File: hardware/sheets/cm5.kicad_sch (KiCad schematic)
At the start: 30 parts, among them J3 microSD, J4 RJ45 GbE magjack UDE RB1-125B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, J40 Fan GND/5V/TACH/PWM, J41 OLED GND/VCC/SCL/SDA, J5 USB-C rpiboot, J6 nRPIBOOT, J7 UART0 GND/TX/RX, M1 CM5002016, Q1 2N7002, SW1 DIP x8, U52 TPS22965DSGR

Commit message: design v2: wireless brain box (C22-C23) — no Ethernet, no buzzer, passive cooler, hinged lid, Wi-Fi AP + QR + phone page, fabrication guide
hardware: 136x100 outline, CM5 wireless antenna edge on the left board edge with a copper-free
strip (rule area), DIN/USB-C/microSD on the right wall, M.2 along the front under the lid, lid
microswitch, CR2032 + service headers on the bottom; magjack and buzzer removed from the
netlist; check_place clean, DRC 0 errors; schematic + connections regenerated, render script
also exports the schematic
software: wifi.py (nmcli / simulated backends, ephemeral key, join, resets), webui.py (stdlib
HTTP phone page: status, certificates, log, join, reset), qr.py, OLED frames with the Wi-Fi QR
code, DIP mode 110 = SERVICE, braindrain wifi-reset; 74 tests, ruff clean; qrcode dependency
enclosure: hinged lid (rear knuckles, filament pin, front snap latch), vents on the antenna side
and front, right-wall cutouts, lid-open scene render
docs: C22/C23, FABRICATION.md (vendors, cost estimate, gates), STATUS R19-R20, panels rear/right,
OLED Wi-Fi mockup, README/ARCHITECTURE/USAGE/BOM/CHANGELOG/HISTORY/tracker updated

Co-Authored-By: Claude Fable 5.1 <noreply@anthropic.com>
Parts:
- removed R10, R11: 10k, Resistor_SMD:R_0402_1005Metric, symbol Device:R
- removed R2, R3: 1k, Resistor_SMD:R_0603_1608Metric, symbol Device:R
- removed R4: 1k, Resistor_SMD:R_0402_1005Metric, symbol Device:R
- removed R5: 100k, Resistor_SMD:R_0402_1005Metric, symbol Device:R
- removed R6, R7: 470, Resistor_SMD:R_0402_1005Metric, symbol Device:R
- BT1: renamed from J41; value OLED GND/VCC/SCL/SDA -> CR2032; footprint Connector_PinHeader_2.54mm:PinHeader_1x04_P2.54mm_Vertical -> Battery:BatteryHolder_Keystone_1060_1x2032; symbol Connector_Generic:Conn_01x04 -> Device:Battery_Cell
- C1: renamed from BT1; value CR2032 -> 22u 10V; footprint Battery:BatteryHolder_Keystone_1060_1x2032 -> Capacitor_SMD:C_0805_2012Metric; symbol Device:Battery_Cell -> Device:C
- C2: renamed from J6; value nRPIBOOT -> 22u 10V; footprint Connector_PinHeader_2.54mm:PinHeader_1x02_P2.54mm_Vertical -> Capacitor_SMD:C_0805_2012Metric; symbol Connector_Generic:Conn_01x02 -> Device:C
- C3: renamed from C1; value 22u 10V -> 10u 10V
- C4: renamed from C2; value 22u 10V -> 1u 10V; footprint Capacitor_SMD:C_0805_2012Metric -> Capacitor_SMD:C_0402_1005Metric
- D1: renamed from C3; value 10u 10V -> green PWR; footprint Capacitor_SMD:C_0805_2012Metric -> LED_THT:LED_D3.0mm; symbol Device:C -> Device:LED
- D2: renamed from C4; value 1u 10V -> green ACT; footprint Capacitor_SMD:C_0402_1005Metric -> LED_THT:LED_D3.0mm; symbol Device:C -> Device:LED
- D3: renamed from D1; value green PWR -> red STATUS
- J40: renamed from SW1; value DIP x8 -> Fan GND/5V/TACH/PWM; footprint Button_Switch_THT:SW_DIP_SPSTx08_Piano_10.8x21.88mm_W7.62mm_P2.54mm -> Connector:FanPinHeader_1x04_P2.54mm_Vertical; symbol Switch:SW_DIP_x08 -> Connector_Generic:Conn_01x04
- J41: renamed from Q1; value 2N7002 -> OLED GND/VCC/SCL/SDA; footprint Package_TO_SOT_SMD:SOT-23 -> Connector_PinHeader_2.54mm:PinHeader_1x04_P2.54mm_Vertical; symbol Transistor_FET:2N7002 -> Connector_Generic:Conn_01x04
- J6: renamed from J7; value UART0 GND/TX/RX -> nRPIBOOT; footprint Connector_PinHeader_2.54mm:PinHeader_1x03_P2.54mm_Vertical -> Connector_PinHeader_2.54mm:PinHeader_1x02_P2.54mm_Vertical; symbol Connector_Generic:Conn_01x03 -> Connector_Generic:Conn_01x02
- J7: renamed from J40; value Fan GND/5V/TACH/PWM -> UART0 GND/TX/RX; footprint Connector:FanPinHeader_1x04_P2.54mm_Vertical -> Connector_PinHeader_2.54mm:PinHeader_1x03_P2.54mm_Vertical; symbol Connector_Generic:Conn_01x04 -> Connector_Generic:Conn_01x03
- R1: renamed from D2; value green ACT -> 1k; footprint LED_THT:LED_D3.0mm -> Resistor_SMD:R_0603_1608Metric; symbol Device:LED -> Device:R
- R10: renamed from D3; value red STATUS -> 10k; footprint LED_THT:LED_D3.0mm -> Resistor_SMD:R_0402_1005Metric; symbol Device:LED -> Device:R
- R11: renamed from D4; value 1N4148W -> 10k; footprint Diode_SMD:D_SOD-123 -> Resistor_SMD:R_0402_1005Metric; symbol Device:D -> Device:R
- R2: renamed from BZ1; value 5V magnetic -> 1k; footprint Buzzer_Beeper:Buzzer_12x9.5RM7.6 -> Resistor_SMD:R_0603_1608Metric; symbol Device:Buzzer -> Device:R
- SW1: renamed from U52; value TPS22965DSGR -> DIP x8; footprint Package_SON:Texas_DSG0008A_WSON-8-1EP_2x2mm_P0.5mm_EP0.9x1.6mm -> Button_Switch_THT:SW_DIP_SPSTx08_Piano_10.8x21.88mm_W7.62mm_P2.54mm; symbol brain-drain:TPS22965 -> Switch:SW_DIP_x08
- U52: renamed from J4; value RJ45 GbE magjack UDE RB1-125B8G1A -> TPS22965DSGR; footprint Connector_RJ:RJ45_UDE_RB1-125B8G1A -> Package_SON:Texas_DSG0008A_WSON-8-1EP_2x2mm_P0.5mm_EP0.9x1.6mm; symbol Connector:RJ45_RB1-125B8G1A -> brain-drain:TPS22965
- renumbered R1 to R3
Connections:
- net Q1_GATE is gone; now on net GND: J41.1 (Pin_1)
- net +3V3: now also C4.1, J41.2 (Pin_2), R1.1, R10.1, R11.1, R2.1, U52.1 (VIN), U52.2 (VIN), U52.4 (VBIAS); no longer BT1.2 (Pin_2), D2.1, SW1.1 (VIN), SW1.2 (VIN), SW1.4 (VBIAS)
- net 5V_SYS: now also C1.1, C2.1, J40.2 (Pin_2); no longer C3.1, C4.1, J7.2 (Pin_2), R11.1 (K), R2.1 (+)
- net D1_A: now also D1.2 (A), R1.2; no longer D3.2 (A), R3.2
- net D2_A: now also D2.2 (A), R2.2; no longer R1.2 (A)
- net D3_A: now also D3.2 (A), R3.2; no longer R10.2 (A)
- net DIP1: now also SW1.1; no longer J40.1
- net DIP2: now also SW1.2; no longer J40.2
- net DIP3: now also SW1.3; no longer J40.3
- net DIP4: now also SW1.4; no longer J40.4
- net DIP5: now also SW1.5; no longer J40.5
- net DIP6: now also SW1.6; no longer J40.6
- net DIP7: now also SW1.7; no longer J40.7
- net DIP8: now also SW1.8; no longer J40.8
- net FAN_PWM: now also J40.4 (Pin_4), R10.2; no longer J7.4 (Pin_4)
- net FAN_TACHO: now also J40.3 (Pin_3); no longer J7.3 (Pin_3)
- net GND: now also BT1.2 (-), D1.1 (K), J40.1 (Pin_1), J6.2 (Pin_2), SW1.10, SW1.11, SW1.12, SW1.13, SW1.14, SW1.15, SW1.16, U52.5 (GND), U52.9 (EP); no longer BT1.1 (Pin_1), D1.2, D2.2, D3.1 (K), J40.10, J40.11, J40.12, J40.13, J40.14, J40.15, J40.16, J40.9, J41.2 (S), J6.1 (Pin_1), SW1.5 (GND), U52.R10 (GND), U52.SH
- net I2C1_SCL: now also J41.3 (Pin_3); no longer BT1.3 (Pin_3)
- net I2C1_SDA: now also J41.4 (Pin_4); no longer BT1.4 (Pin_4)
- net LED_nACT: now also D2.1 (K); no longer R1.1 (K)
- net SD_PWR_ON: now also R11.2, U52.3 (ON); no longer SW1.3 (ON)
- net SD_VDD: now also C3.1, U52.7 (VOUT), U52.8 (VOUT); no longer D1.1, SW1.7 (VOUT), SW1.8 (VOUT)
- net STATUS_LED: now also D3.1 (K); no longer R10.1 (K)
- net UART0_RXD: now also J7.3 (Pin_3); no longer J6.3 (Pin_3)
- net UART0_TXD: now also J7.2 (Pin_2); no longer J6.2 (Pin_2)
- net VBAT: now also BT1.1 (+); no longer C1.1 (+)
- net nRPIBOOT: now also J6.1 (Pin_1); no longer C2.1 (Pin_1)
- net BUZZER: no longer names the net of M1.49 (GPIO18)
- removed net BZ1_N: J41.3 (D), R11.2 (A), R2.2 (-)
- removed net ETH_LED_G_A: U52.L1
- removed net ETH_LED_Y_A: U52.L3
- net ETH_P0_N: no longer names the net of M1.10 (Ethernet_Pair0_N)
- net ETH_P0_N: no longer U52.R3 (TD1-)
- net ETH_P0_P: no longer names the net of M1.12 (Ethernet_Pair0_P)
- net ETH_P0_P: no longer U52.R2 (TD1+)
- net ETH_P1_N: no longer names the net of M1.6 (Ethernet_Pair1_N)
- net ETH_P1_N: no longer U52.R5 (TD2-)
- net ETH_P1_P: no longer names the net of M1.4 (Ethernet_Pair1_P)
- net ETH_P1_P: no longer U52.R4 (TD2+)
- net ETH_P2_N: no longer names the net of M1.9 (Ethernet_Pair2_N)
- net ETH_P2_N: no longer U52.R7 (TD3-)
- net ETH_P2_P: no longer names the net of M1.11 (Ethernet_Pair2_P)
- net ETH_P2_P: no longer U52.R6 (TD3+)
- net ETH_P3_N: no longer names the net of M1.5 (Ethernet_Pair3_N)
- net ETH_P3_N: no longer U52.R9 (TD4-)
- net ETH_P3_P: no longer names the net of M1.3 (Ethernet_Pair3_P)
- net ETH_P3_P: no longer U52.R8 (TD4+)
- net ETH_nLED2: no longer names the net of M1.17 (Ethernet_nLED2)
- net ETH_nLED2: no longer U52.L4
- net ETH_nLED3: no longer names the net of M1.15 (Ethernet_nLED3)
- net ETH_nLED3: no longer U52.L2
- no-connect marks 77 -> 87
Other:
- note added: "Ethernet dropped (C22). The CM5 wireless variant's PCB antenna is on the short module edge that carries MH1; that edge sits on the board's left edge with an 8 mm copper-free strip under it and no metal within 10 mm (CM5 datasheet 4.1.2)."
- note added: "cm5: Compute Module 5 (wireless): power, control, GPIO, microSD, USB-C, UART, RTC cell, fan, DIP, LEDs, OLED"
- note removed: "CM5IO reference adds TPD4EUSB30 ESD arrays on the Ethernet pairs; omitted here (indoor appliance), add if the board sees external cabling abuse."
- note removed: "Magjack: UDE RB1-125B8G1A (the only 1000BASE-T magjack in the stock library). CM5 pair0..3 -> TD1..TD4; verify pair order and LED anode/cathode (L1..L4) against the UDE drawing. Centre tap left unconnected pending the CM5IO reference schematic."
- note removed: "cm5: Compute Module 5: power, control, GPIO, microSD, Ethernet, USB-C, UART, RTC cell, fan, DIP, LEDs, buzzer, OLED"
- moved on the sheet: C3, C4, D3, R3

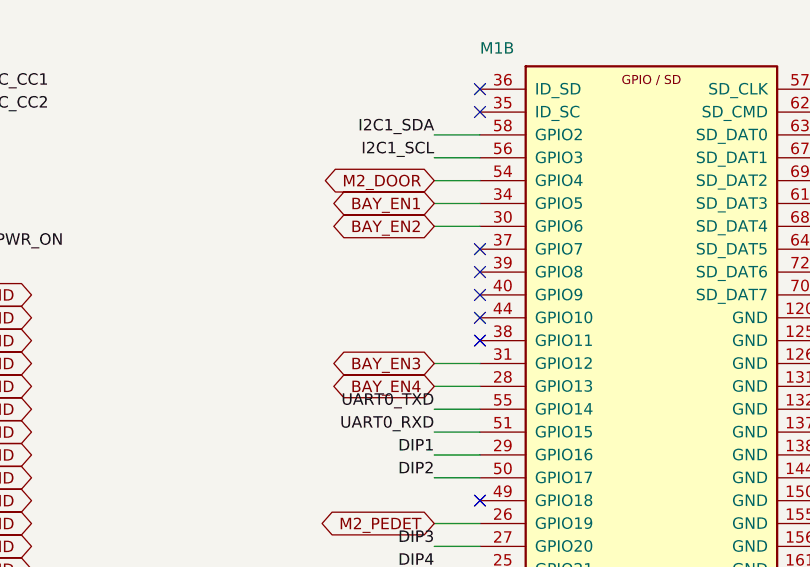
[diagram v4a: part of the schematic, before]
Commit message: docs: C24 brain + bay cards — decisions, architecture, BOM card table, fabrication, README, USAGE, STATUS, changelog, history; diagrams: 8 slots, lid plan, left wall
Co-Authored-By: Claude Fable 5.1 <noreply@anthropic.com>
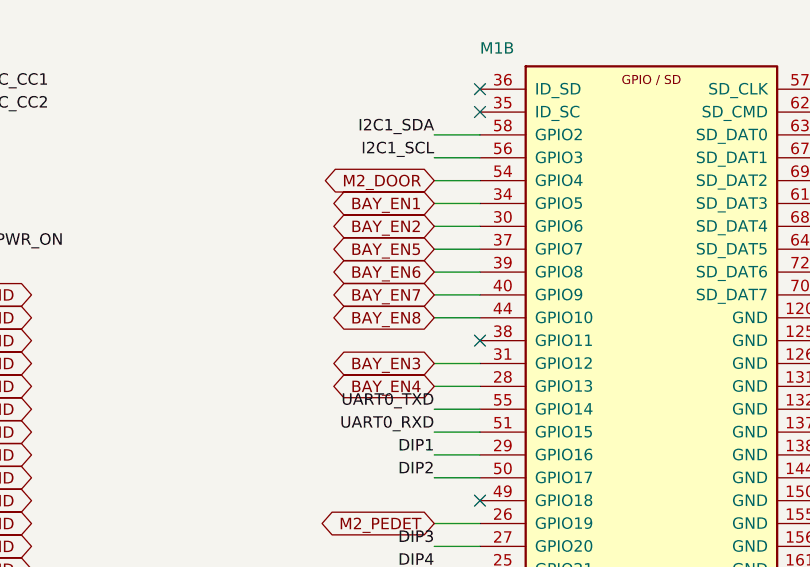
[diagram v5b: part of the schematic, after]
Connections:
- net BAY_EN5: now reaches M1.37 (GPIO7)
- net BAY_EN6: now reaches M1.39 (GPIO8)
- net BAY_EN7: now reaches M1.40 (GPIO9)
- net BAY_EN8: now reaches M1.44 (GPIO10)
- no-connect marks 87 -> 83
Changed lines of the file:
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@@
+		)
+	)
+	(wire
+		(pts
+			(xy 181.61 50.8)
+			(xy 176.53 50.8)
+		)
+		(stroke
+			(width 0)
+			(type default)
+		)
+	)
+	(global_label "BAY_EN5"
+		(shape bidirectional)
+		(at 176.53 50.8 180)
+		(fields_autoplaced yes)
+		(effects
+			(font
+				(size 1.27 1.27)
+			)
+			(justify right)
+		)
+		(property "Intersheetrefs" "${INTERSHEET_REFS}"
+			(at 176.53 50.8 0)
+			(effects
+				(font
+					(size 1.27 1.27)
+				)
+				(hide yes)
+			)
+		)
+	)
+	(wire
+		(pts
+			(xy 181.61 53.34)
+			(xy 176.53 53.34)
+		)
+		(stroke
+			(width 0)
+			(type default)
+		)
+	)
+	(global_label "BAY_EN6"
+		(shape bidirectional)
+		(at 176.53 53.34 180)
+		(fields_autoplaced yes)
+		(effects
+			(font
+				(size 1.27 1.27)
+			)
+			(justify right)
+		)
+		(property "Intersheetrefs" "${INTERSHEET_REFS}"
+			(at 176.53 53.34 0)
+			(effects
+				(font
+					(size 1.27 1.27)
+				)
+				(hide yes)
+			)
+		)
+	)
+	(wire
+		(pts
+			(xy 181.61 55.88)
+			(xy 176.53 55.88)
+		)
+		(stroke
+			(width 0)
+			(type default)
+		)
+	)
+	(global_label "BAY_EN7"
+		(shape bidirectional)
+		(at 176.53 55.88 180)
+		(fields_autoplaced yes)
+		(effects
+			(font
+				(size 1.27 1.27)
+			)
+			(justify right)
+		)
+		(property "Intersheetrefs" "${INTERSHEET_REFS}"
+			(at 176.53 55.88 0)
+			(effects
+				(font
+					(size 1.27 1.27)
+				)
+				(hide yes)
+			)
+		)
+	)
+	(wire
+		(pts
+			(xy 181.61 58.42)
+			(xy 176.53 58.42)
+		)
+		(stroke
+			(width 0)
+			(type default)
+		)
+	)
+	(global_label "BAY_EN8"
+		(shape bidirectional)
+		(at 176.53 58.42 180)
+		(fields_autoplaced yes)
+		(effects
+			(font
+				(size 1.27 1.27)
+			)
+			(justify right)
+		)
+		(property "Intersheetrefs" "${INTERSHEET_REFS}"
+			(at 176.53 58.42 0)
+			(effects
+				(font
+					(size 1.27 1.27)
+				)
+				(hide yes)
+			)
 		)
 	)
 	(no_connect
-		(at 181.61 50.8)
-	)
-	(no_connect
-		(at 181.61 53.34)
-	)
-	(no_connect
-		(at 181.61 55.88)
-	)
-	(no_connect
-		(at 181.61 58.42)
-	)
-	(no_connect
